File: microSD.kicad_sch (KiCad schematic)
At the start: 7 parts, among them J4 Micro_SD_Card

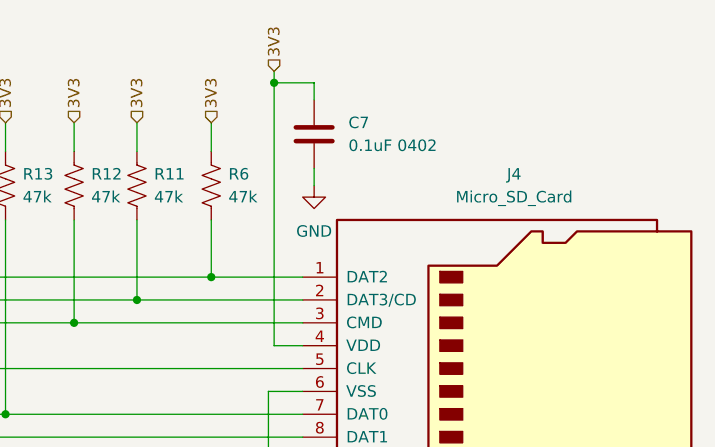
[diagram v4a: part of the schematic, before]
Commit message: adding script to pull prices and availability from Mouser
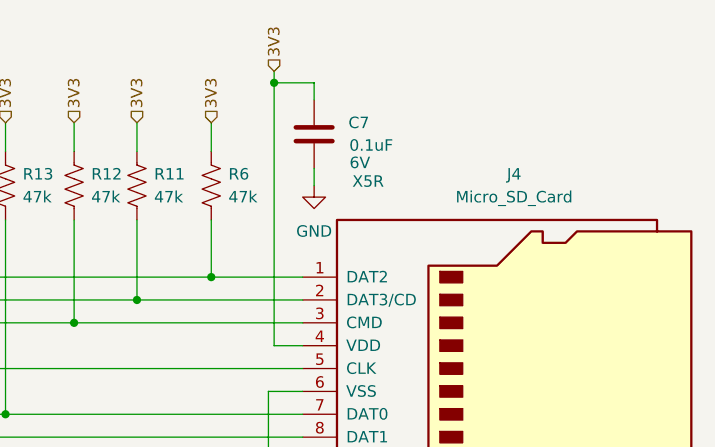
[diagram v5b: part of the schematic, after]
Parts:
- C7: value 0.1uF 0402 -> 0.1uF; Type (none) -> X5R; Voltage (none) -> 6V
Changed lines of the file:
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@@
   )
   (symbol (lib_id "Device:C") (at 153.67 60.325 0) (unit 1)
-    (in_bom yes) (on_board yes) (dnp no) (fields_autoplaced)
+    (in_bom yes) (on_board yes) (dnp no)
     (property "Reference" "C7" (at 157.48 59.055 0)
       (effects (font (size 1.27 1.27)) (justify left))
     )
-    (property "Value" "0.1uF 0402" (at 157.48 61.595 0)
+    (property "Value" "0.1uF" (at 157.5765 61.565 0)
       (effects (font (size 1.27 1.27)) (justify left))
     )
@@
       (effects (font (size 1.27 1.27)) hide)
     )
+    (property "Voltage" "6V" (at 158.75 63.5 0)
+      (effects (font (size 1.27 1.27)))
+    )
+    (property "Type" "X5R" (at 159.674 65.5694 0)
+      (effects (font (size 1.27 1.27)))
+    )
     (pin "1")

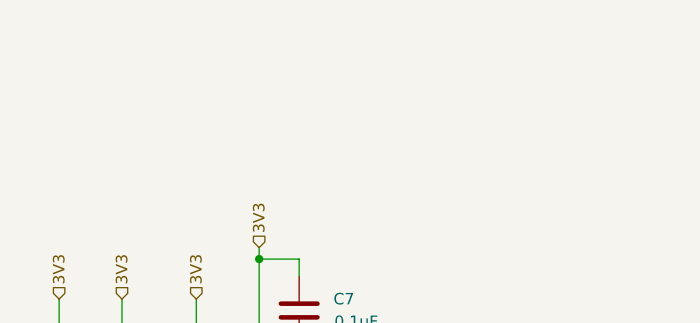
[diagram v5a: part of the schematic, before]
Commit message: script working to generate Mouser, Digikey, and JLPCB BOMS
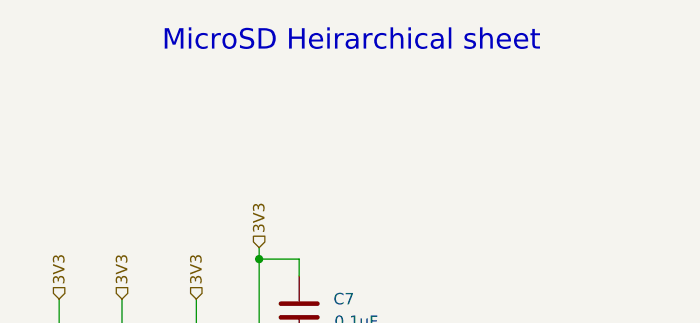
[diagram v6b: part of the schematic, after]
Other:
- note added: "MicroSD Heirarchical sheet"
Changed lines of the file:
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@@
     (stroke (width 0) (type default))
+  )
+  (text "MicroSD Heirarchical sheet" (at 138.43 31.75 0)
+    (effects (font (size 2.27 2.27)) (justify left bottom))
   )
   (hierarchical_label "D2" (shape bidirectional) (at 104.14 76.2 180) (fields_autoplaced)
